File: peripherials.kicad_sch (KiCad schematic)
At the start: 53 parts, among them U15 PN7160AHN

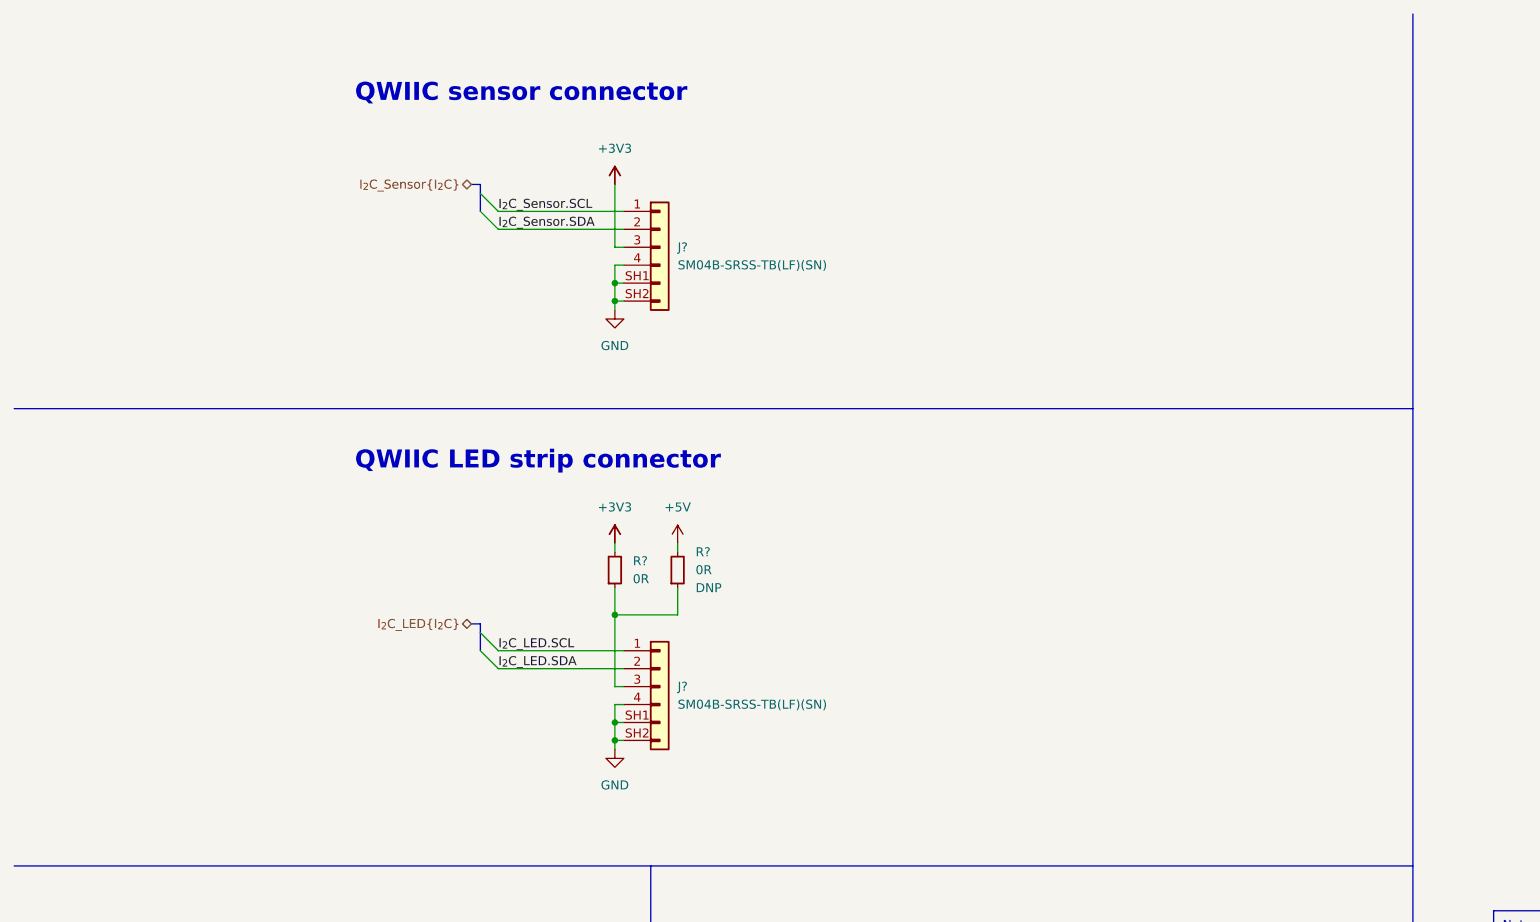
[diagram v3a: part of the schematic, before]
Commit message: [#54447] Fix pin order of Sensor&LED connectors; add ESD protection to these conns
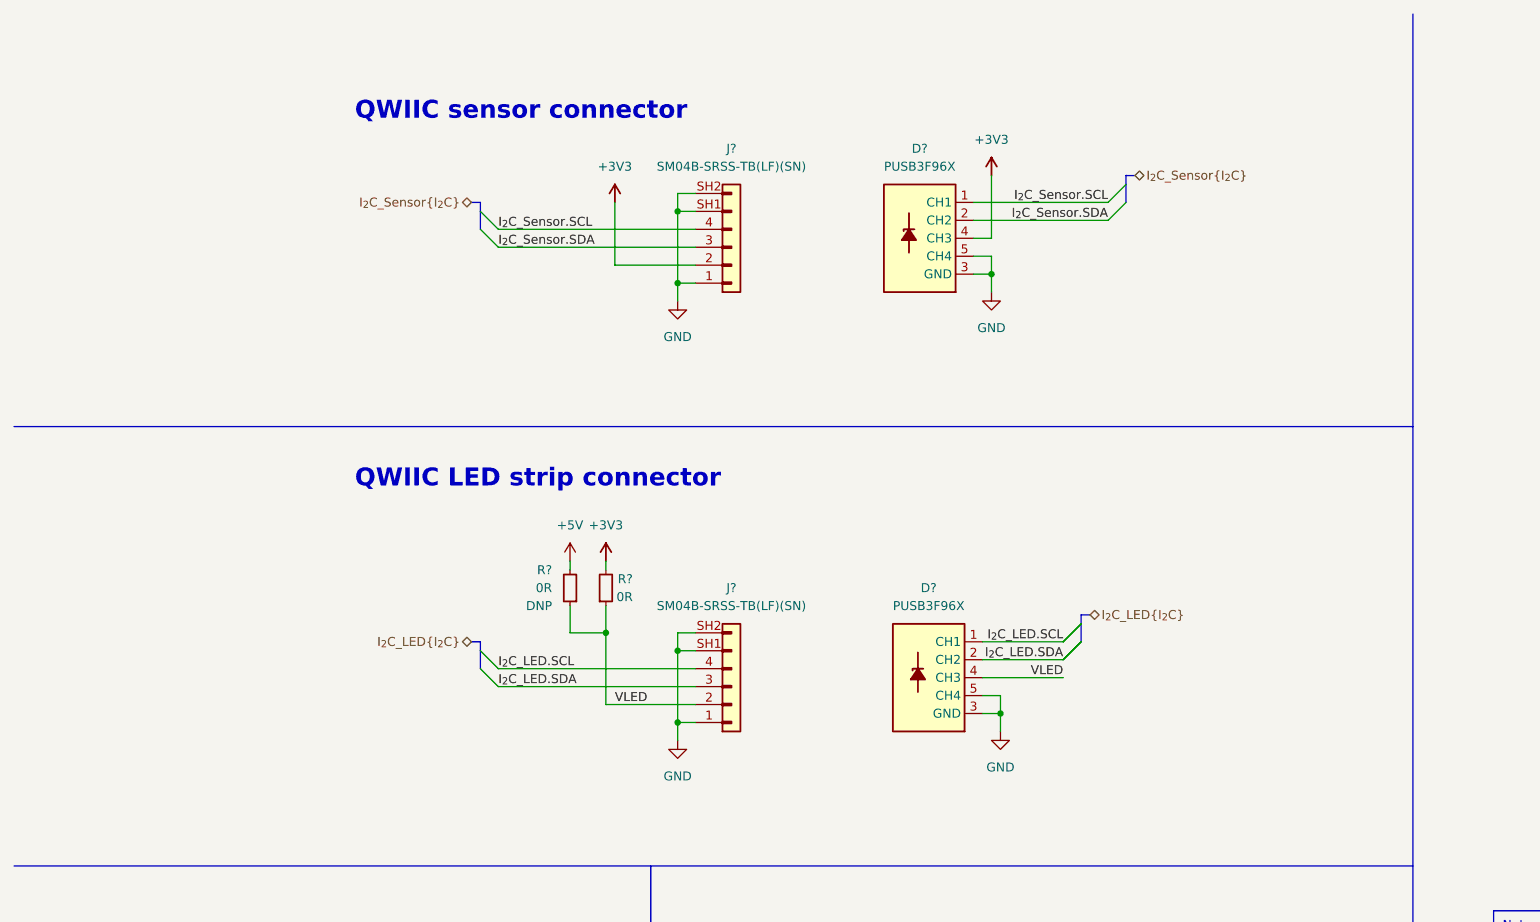
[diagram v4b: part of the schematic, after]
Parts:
- removed J? (x2): JST_SH_1x4_SM04B-SRSS-TB-LF-SN, antmicro-footprints:Conn_JST_SH_1x4_SM04B-SRSS-TB-LF-SN, symbol antmicroWire2BoardConnectors:JST_SH_1x4_SM04B-SRSS-TB-LF-SN
- removed R? (x2): R_0R_0402, antmicro-footprints:R_0402_1005Metric, symbol antmicroResistors0402:R_0R_0402
- added D? (x2): PUSB3F96X_PASS, antmicro-footprints:Nexperia_DFN-10_2.5x1mm_P0.5mm, symbol antmicroTVSDiodes:PUSB3F96X_PASS
- added J? (x2): JST_SH_1x4_SM04B-SRSS-TB-LF-SN, antmicro-footprints:Conn_JST_SH_1x4_SM04B-SRSS-TB-LF-SN, symbol antmicroWire2BoardConnectors:JST_SH_1x4_SM04B-SRSS-TB-LF-SN
- added R? (x2): R_0R_0402, antmicro-footprints:R_0402_1005Metric, symbol antmicroResistors0402:R_0R_0402
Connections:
- net +3V3: now also D?.4 (CH3), D?.7 (CH3), J?.2, R?.2
- net +5V: now also R?.2
- net GND: now also D?.3 (GND), D?.3 (GND), D?.5 (CH4), D?.5 (CH4), D?.6 (CH4), D?.6 (CH4), D?.8 (GND), D?.8 (GND), J?.1, J?.1, J?.SH1, J?.SH1, J?.SH2, J?.SH2
- net I_{2}C_LED.SCL: now also D?.1 (CH1), D?.10 (CH1), J?.4
- net I_{2}C_LED.SDA: now also D?.2 (CH2), D?.9 (CH2), J?.3
- net I_{2}C_Sensor.SCL: now also D?.1 (CH1), D?.10 (CH1), J?.4
- net I_{2}C_Sensor.SDA: now also D?.2 (CH2), D?.9 (CH2), J?.3
- new net VLED: D?.4 (CH3), D?.7 (CH3), J?.2, R?.1, R?.1

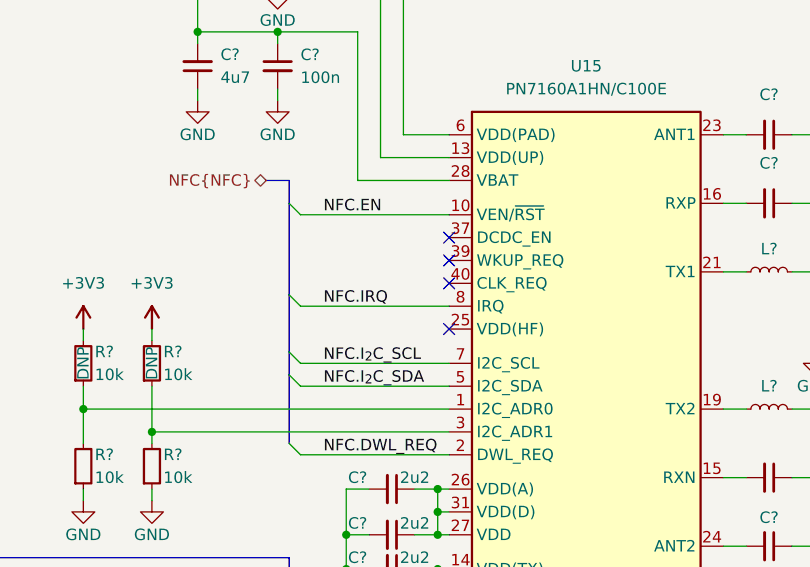
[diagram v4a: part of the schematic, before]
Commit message: [#54447] Add testpoints to unused pins of PN7160
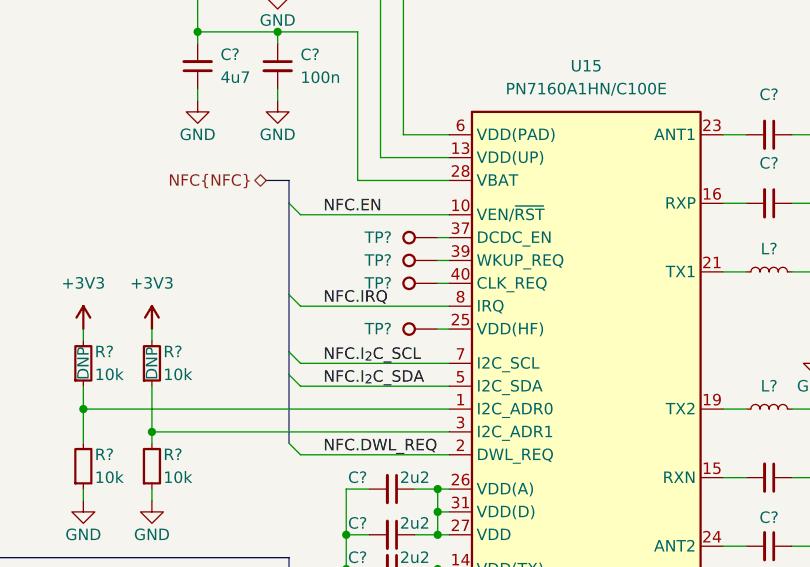
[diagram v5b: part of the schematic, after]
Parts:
- added TP? (x4): TP_1mm_SMD, antmicro-footprints:TP_SMD_1mm, symbol antmicroTestPoints:TP_1mm_SMD
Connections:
- net at U15.25 (VDD(HF)): now also TP?.1
- net at U15.37 (DCDC_EN): now also TP?.1
- net at U15.39 (WKUP_REQ): now also TP?.1
- net at U15.40 (CLK_REQ): now also TP?.1
- no-connect marks 4 -> 0
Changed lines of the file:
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@@
   (junction (at 265.43 137.16) (diameter 0) (color 0 0 0 0)
   )
-  (no_connect (at 276.86 104.14))
-  (no_connect (at 276.86 106.68))
-  (no_connect (at 276.86 114.3))
-  (no_connect (at 276.86 109.22))
   (bus_entry (at 24.13 189.23) (size 2.54 2.54)
     (stroke (width 0) (type default) (color 0 0 0 0))
@@
     (stroke (width 0) (type default) (color 0 0 0 0))
   )
+  (wire (pts (xy 275.59 114.3) (xy 276.86 114.3))
+    (stroke (width 0) (type default) (color 0 0 0 0))
+  )
   (wire (pts (xy 307.34 138.43) (xy 309.88 138.43))
     (stroke (width 0) (type default) (color 0 0 0 0))
@@
     (stroke (width 0) (type default) (color 0 0 0 0))
   )
+  (wire (pts (xy 275.59 106.68) (xy 276.86 106.68))
+    (stroke (width 0) (type default) (color 0 0 0 0))
+  )
   (wire (pts (xy 132.08 210.82) (xy 114.3 210.82))
     (stroke (width 0) (type default) (color 0 0 0 0))
@@
     (stroke (width 0) (type default) (color 0 0 0 0))
   )
+  (wire (pts (xy 275.59 104.14) (xy 276.86 104.14))
+    (stroke (width 0) (type default) (color 0 0 0 0))
+  )
   (wire (pts (xy 58.42 201.93) (xy 58.42 219.71))
     (stroke (width 0) (type default) (color 0 0 0 0))
@@
     (stroke (width 0) (type default) (color 0 0 0 0))
   )
+  (wire (pts (xy 275.59 109.22) (xy 276.86 109.22))
+    (stroke (width 0) (type default) (color 0 0 0 0))
+  )
   (bus (pts (xy 78.74 101.6) (xy 78.74 102.87))
     (stroke (width 0) (type default) (color 0 0 0 0))
@@
     (pin "1")
   )
+  (symbol (lib_id "antmicroTestPoints:TP_1mm_SMD") (at 275.59 114.3 180) (unit 1)
+    (in_bom yes) (on_board yes) (fields_autoplaced)
+    (property "Reference" "TP?" (id 0) (at 270.51 114.2999 0)
+      (effects (font (size 1.27 1.27) (thickness 0.15)) (justify left))
+    )
+    (property "Value" "TP_1mm_SMD" (id 1) (at 260.35 106.68 0)
+      (effects (font (size 1.27 1.27) (thickness 0.15)) (justify left bottom) hide)
+    )
+    (property "Footprint" "antmicro-footprints:TP_SMD_1mm" (id 2) (at 260.35 104.14 0)
+      (effects (font (size 1.27 1.27) (thickness 0.15)) (justify left bottom) hide)
+    )
+    (property "Datasheet" "" (id 3) (at 260.35 101.6 0)
+      (effects (font (size 1.27 1.27) (thickness 0.15)) (justify left bottom) hide)
+    )
+    (property "Author" "Antmicro" (id 4) (at 260.35 99.06 0)
+      (effects (font (size 1.27 1.27) (thickness 0.15)) (justify left bottom) hide)
+    )
+    (property "License" "Apache-2.0" (id 5) (at 260.35 96.52 0)
+      (effects (font (size 1.27 1.27) (thickness 0.15)) (justify left bottom) hide)
+    )
+    (property "MPN" "" (id 6) (at 275.59 114.3 0)
+      (effects (font (size 1.27 1.27)) hide)
+    )
+    (property "Manufacturer" "" (id 7) (at 275.59 114.3 0)
+      (effects (font (size 1.27 1.27)) hide)
+    )
+    (pin "1")
+  )
   (symbol (lib_id "antmicroCapacitors0402:C_template_name_0402") (at 322.58 121.92 90) (unit 1)
     (in_bom yes) (on_board yes)
@@
     (pin "2")
   )
+  (symbol (lib_id "antmicroTestPoints:TP_1mm_SMD") (at 275.59 104.14 180) (unit 1)
+    (in_bom yes) (on_board yes) (fields_autoplaced)
+    (property "Reference" "TP?" (id 0) (at 270.51 104.1399 0)
+      (effects (font (size 1.27 1.27) (thickness 0.15)) (justify left))
+    )
+    (property "Value" "TP_1mm_SMD" (id 1) (at 260.35 96.52 0)
+      (effects (font (size 1.27 1.27) (thickness 0.15)) (justify left bottom) hide)
+    )
+    (property "Footprint" "antmicro-footprints:TP_SMD_1mm" (id 2) (at 260.35 93.98 0)
+      (effects (font (size 1.27 1.27) (thickness 0.15)) (justify left bottom) hide)
+    )
+    (property "Datasheet" "" (id 3) (at 260.35 91.44 0)
+      (effects (font (size 1.27 1.27) (thickness 0.15)) (justify left bottom) hide)
+    )
+    (property "Author" "Antmicro" (id 4) (at 260.35 88.9 0)
+      (effects (font (size 1.27 1.27) (thickness 0.15)) (justify left bottom) hide)
+    )
+    (property "License" "Apache-2.0" (id 5) (at 260.35 86.36 0)
+      (effects (font (size 1.27 1.27) (thickness 0.15)) (justify left bottom) hide)
+    )
+    (property "MPN" "" (id 6) (at 275.59 104.14 0)
+      (effects (font (size 1.27 1.27)) hide)
+    )
+    (property "Manufacturer" "" (id 7) (at 275.59 104.14 0)
+      (effects (font (size 1.27 1.27)) hide)
+    )
+    (pin "1")
+  )
   (symbol (lib_id "antmicroCapacitors0402:C_1u_0402") (at 257.81 62.23 90) (unit 1)
     (in_bom yes) (on_board yes) (fields_autoplaced)
@@
     (pin "2")
   )
+  (symbol (lib_id "antmicroTestPoints:TP_1mm_SMD") (at 275.59 106.68 180) (unit 1)
+    (in_bom yes) (on_board yes) (fields_autoplaced)
+    (property "Reference" "TP?" (id 0) (at 270.51 106.6799 0)
+      (effects (font (size 1.27 1.27) (thickness 0.15)) (justify left))
+    )
+    (property "Value" "TP_1mm_SMD" (id 1) (at 260.35 99.06 0)
+      (effects (font (size 1.27 1.27) (thickness 0.15)) (justify left bottom) hide)
+    )
+    (property "Footprint" "antmicro-footprints:TP_SMD_1mm" (id 2) (at 260.35 96.52 0)
+      (effects (font (size 1.27 1.27) (thickness 0.15)) (justify left bottom) hide)
+    )
+    (property "Datasheet" "" (id 3) (at 260.35 93.98 0)
+      (effects (font (size 1.27 1.27) (thickness 0.15)) (justify left bottom) hide)
+    )
+    (property "Author" "Antmicro" (id 4) (at 260.35 91.44 0)
+      (effects (font (size 1.27 1.27) (thickness 0.15)) (justify left bottom) hide)
+    )
+    (property "License" "Apache-2.0" (id 5) (at 260.35 88.9 0)
+      (effects (font (size 1.27 1.27) (thickness 0.15)) (justify left bottom) hide)
+    )
+    (property "MPN" "" (id 6) (at 275.59 106.68 0)
+      (effects (font (size 1.27 1.27)) hide)
+    )
+    (property "Manufacturer" "" (id 7) (at 275.59 106.68 0)
+      (effects (font (size 1.27 1.27)) hide)
+    )
+    (pin "1")
+  )
   (symbol (lib_id "antmicropower:+5V") (at 58.42 177.8 0) (unit 1)
     (in_bom yes) (on_board yes) (fields_autoplaced)
@@
     (pin "2")
   )
+  (symbol (lib_id "antmicroTestPoints:TP_1mm_SMD") (at 275.59 109.22 180) (unit 1)
+    (in_bom yes) (on_board yes) (fields_autoplaced)
+    (property "Reference" "TP?" (id 0) (at 270.51 109.2199 0)
+      (effects (font (size 1.27 1.27) (thickness 0.15)) (justify left))
+    )
+    (property "Value" "TP_1mm_SMD" (id 1) (at 260.35 101.6 0)
+      (effects (font (size 1.27 1.27) (thickness 0.15)) (justify left bottom) hide)
+    )
+    (property "Footprint" "antmicro-footprints:TP_SMD_1mm" (id 2) (at 260.35 99.06 0)
+      (effects (font (size 1.27 1.27) (thickness 0.15)) (justify left bottom) hide)
+    )
+    (property "Datasheet" "" (id 3) (at 260.35 96.52 0)
+      (effects (font (size 1.27 1.27) (thickness 0.15)) (justify left bottom) hide)
+    )
+    (property "Author" "Antmicro" (id 4) (at 260.35 93.98 0)
+      (effects (font (size 1.27 1.27) (thickness 0.15)) (justify left bottom) hide)
+    )
+    (property "License" "Apache-2.0" (id 5) (at 260.35 91.44 0)
+      (effects (font (size 1.27 1.27) (thickness 0.15)) (justify left bottom) hide)
+    )
+    (property "MPN" "" (id 6) (at 275.59 109.22 0)
+      (effects (font (size 1.27 1.27)) hide)
+    )
+    (property "Manufacturer" "" (id 7) (at 275.59 109.22 0)
+      (effects (font (size 1.27 1.27)) hide)
+    )
+    (pin "1")
+  )
   (symbol (lib_id "antmicroCapacitors0402:C_template_name_0402") (at 342.9 123.19 0) (mirror y) (unit 1)

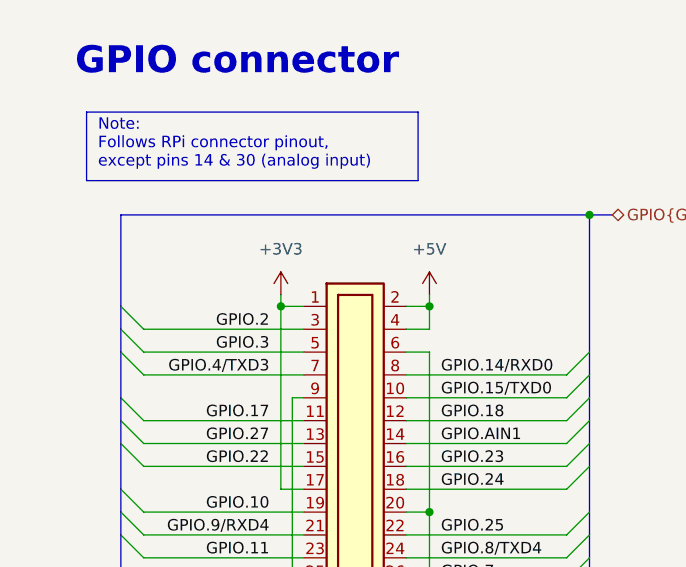
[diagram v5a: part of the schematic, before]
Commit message: [#54474] Complete USB schematics
- merge sch usb&debug
- add USB/4xUART bridge
- add USB-PD managament
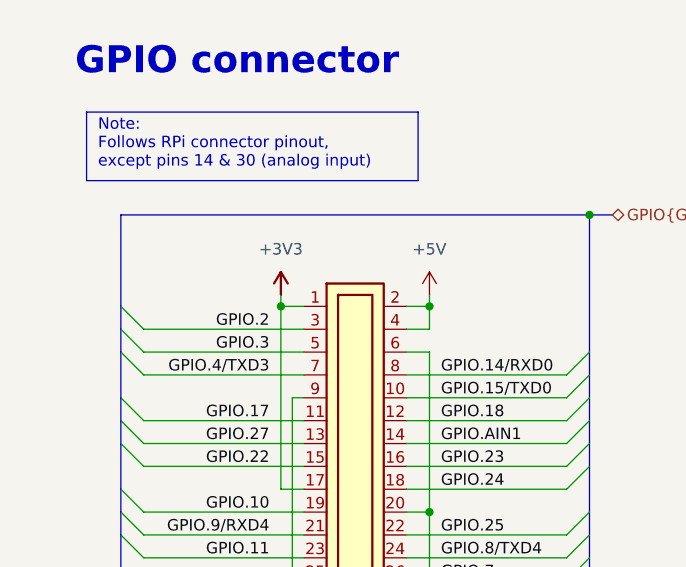
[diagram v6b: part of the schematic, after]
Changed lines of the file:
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@@
     (pin "1")
   )
-  (symbol (lib_name "+3V3_1") (lib_id "antmicropower:+3V3") (at 41.91 177.8 0) (unit 1)
+  (symbol (lib_id "antmicropower:+3V3") (at 41.91 177.8 0) (unit 1)
     (in_bom yes) (on_board yes) (fields_autoplaced)
     (property "Reference" "#PWR?" (id 0) (at 57.15 177.8 0)

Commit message: [#54617] Reduce capacitors diversity
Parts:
- L? (x2): footprint antmicro-footprints: -> antmicro-footprints:L_0402_1005Metric
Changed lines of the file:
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@@
       (effects (font (size 1.27 1.27) (thickness 0.15)) (justify left bottom) hide)
     )
-    (property "Footprint" "antmicro-footprints:" (id 2) (at 323.85 130.81 0)
+    (property "Footprint" "antmicro-footprints:L_0402_1005Metric" (id 2) (at 323.85 130.81 0)
       (effects (font (size 1.27 1.27) (thickness 0.15)) (justify left bottom) hide)
     )
@@
       (effects (font (size 1.27 1.27) (thickness 0.15)) (justify left bottom) hide)
     )
-    (property "Footprint" "antmicro-footprints:" (id 2) (at 323.85 115.57 0)
-      (effects (font (size 1.27 1.27) (thickness 0.15)) (justify left bottom) hide)
-    )
+    (property "Footprint" "antmicro-footprints:L_0402_1005Metric" (id 2) (at 323.85 115.57 0)
+      (effects (font (size 1.27 1.27) (thickness 0.15)) (justify left bottom) hide)
+    )
